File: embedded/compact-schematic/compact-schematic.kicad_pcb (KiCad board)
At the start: 2 copper layers, 50.8 x 30.5 mm, 14 parts, among them Q1 NMOS, Q2 NMOS, Q3 NMOS

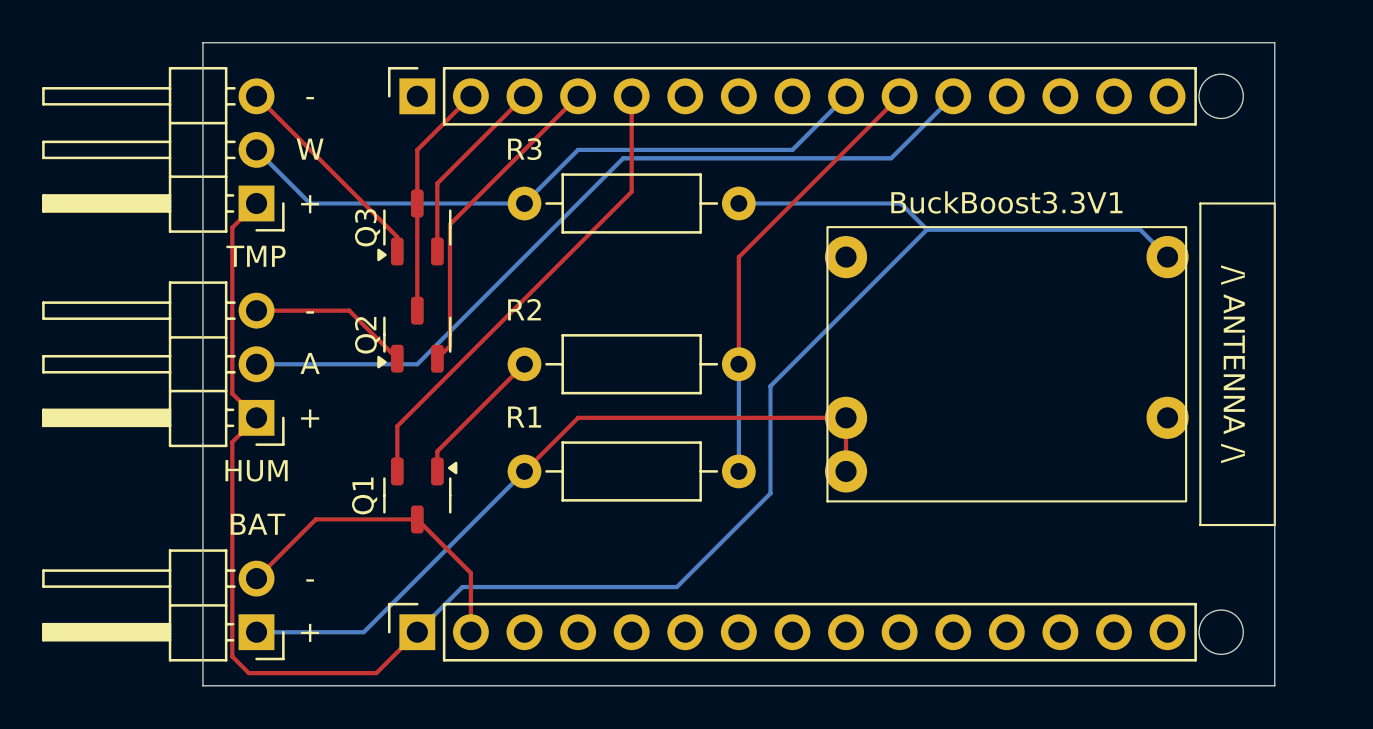
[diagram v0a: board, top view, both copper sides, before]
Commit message: updated compact schematic
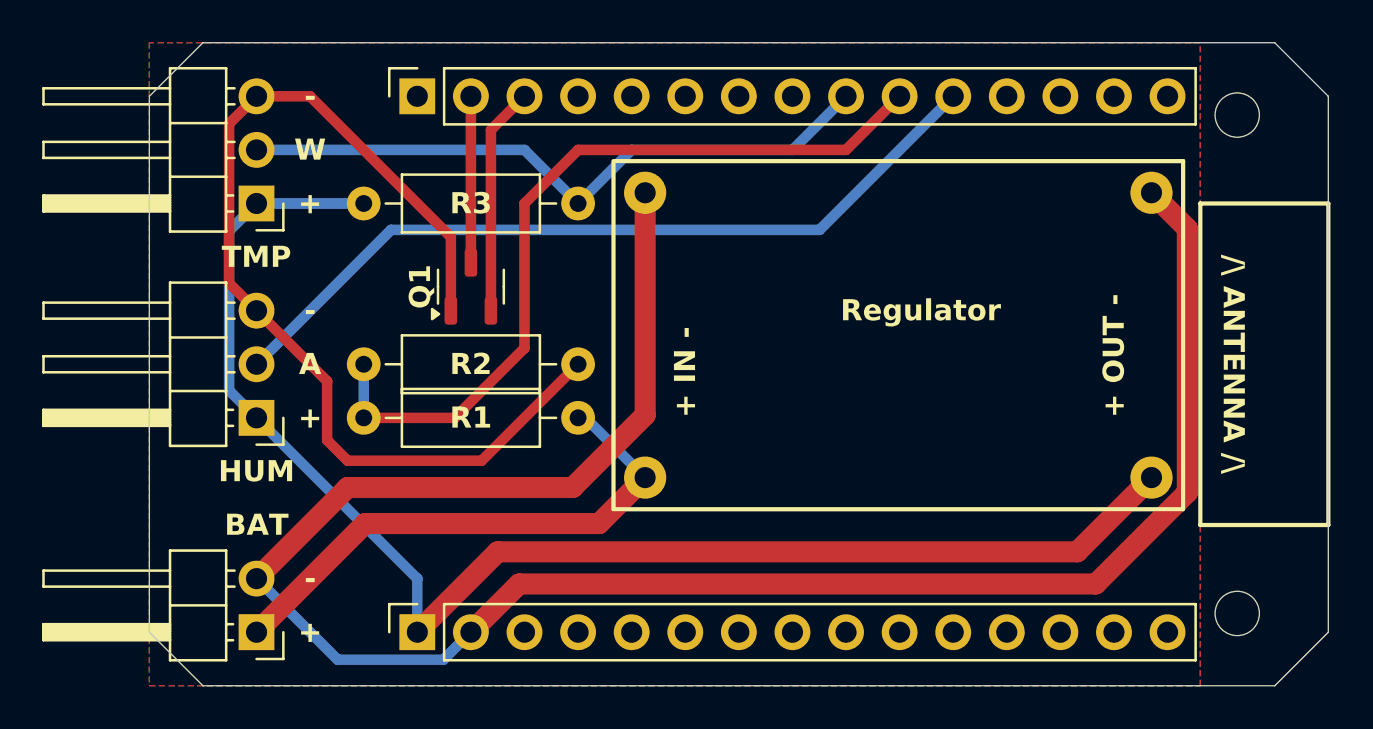
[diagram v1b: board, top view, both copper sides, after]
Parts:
- removed BuckBoost3.3V1: ~, custom:BuckBoost3.3V
- removed Q2, Q3: NMOS, Package_TO_SOT_SMD:SOT-23-3
- added Regulator: ~, custom:BuckBoost3.3V_0.85A, F.Cu at (58.9, 39.5)
- moved R2 17.8 mm to (33.0, 40.6), turned to 0 degrees
- moved R3 17.8 mm to (33.0, 33.0), turned to 0 degrees
- moved Q1 10.2 mm to (38.1, 37.0), turned to 90 degrees
- moved R1 3.59 mm to (43.2, 43.2), turned to 180 degrees
- moved REF** 1.17 mm to (74.4, 52.5)
- moved REF** 1.17 mm to (74.4, 28.8)
- renumbered REF** to BoardLeft, REF** to BoardRight
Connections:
- BoardRight pad 3: TMP_EN -> SEN
- BoardRight pad 4: HUM_EN -> (no net)
- BoardRight pad 5: BAT_EN -> (no net)
- Q1 pad 1: Net-(Q1-D) -> HUM-
- Q1 pad 2: BAT_EN -> SEN
- R2 pad 2: Net-(Q1-D) -> HUM-
- TMP pad 3: TMP- -> HUM-
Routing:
- net GND: track 26.4 -> 104.0 mm
- net HUM-: track 7.61 -> 48.4 mm
- net BAT_EN: track 22.4 -> 0.00 mm
- net 3.3V: track 89.2 -> 67.5 mm
- net BAT: track 20.9 -> 38.3 mm
- net HUM_EN: track 15.2 -> 0.00 mm
- net SEN: track 0.00 -> 10.8 mm
- net TMP-: track 10.1 -> 0.00 mm
- net BAT+: track 35.0 -> 25.8 mm
- net TMP_EN: track 9.07 -> 0.00 mm
- net Net-(Q1-D): track 6.79 -> 0.00 mm
- added copper zone on B.Cu, net GND
- added copper zone on F.Cu, net GND
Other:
- board size 50.8 x 30.5 mm -> 55.9 x 30.5 mm
- board text added: "+ IN -"
- board text added: "+ OUT -"
- board text added: "BAT"
- board text added: "GardenEye"
- board text added: "HUM"
- board text added: "TMP"

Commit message: updated schematic
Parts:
- removed Regulator: ~, custom:BuckBoost3.3V_0.85A
- added Regulator1: ~, custom:BuckBoost3.3V_0.85A, F.Cu at (58.8, 39.3)
- moved REF** 0.22 mm to (74.6, 28.8)
- moved REF** 0.22 mm to (74.6, 52.5)
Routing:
- net GND: track 104.0 -> 105.7 mm
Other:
- board text removed: "+ IN -"
- board text removed: "+ OUT -"
